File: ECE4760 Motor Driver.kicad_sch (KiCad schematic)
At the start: 47 parts, among them J1 IO, J101 Alternative Motor, J2 Motor / Power, J3 UART, U1 STM32G473V_B-C-E_Hx, U6 AP7361C-33FGE, U7 TPSM365R6, X1 48MHz

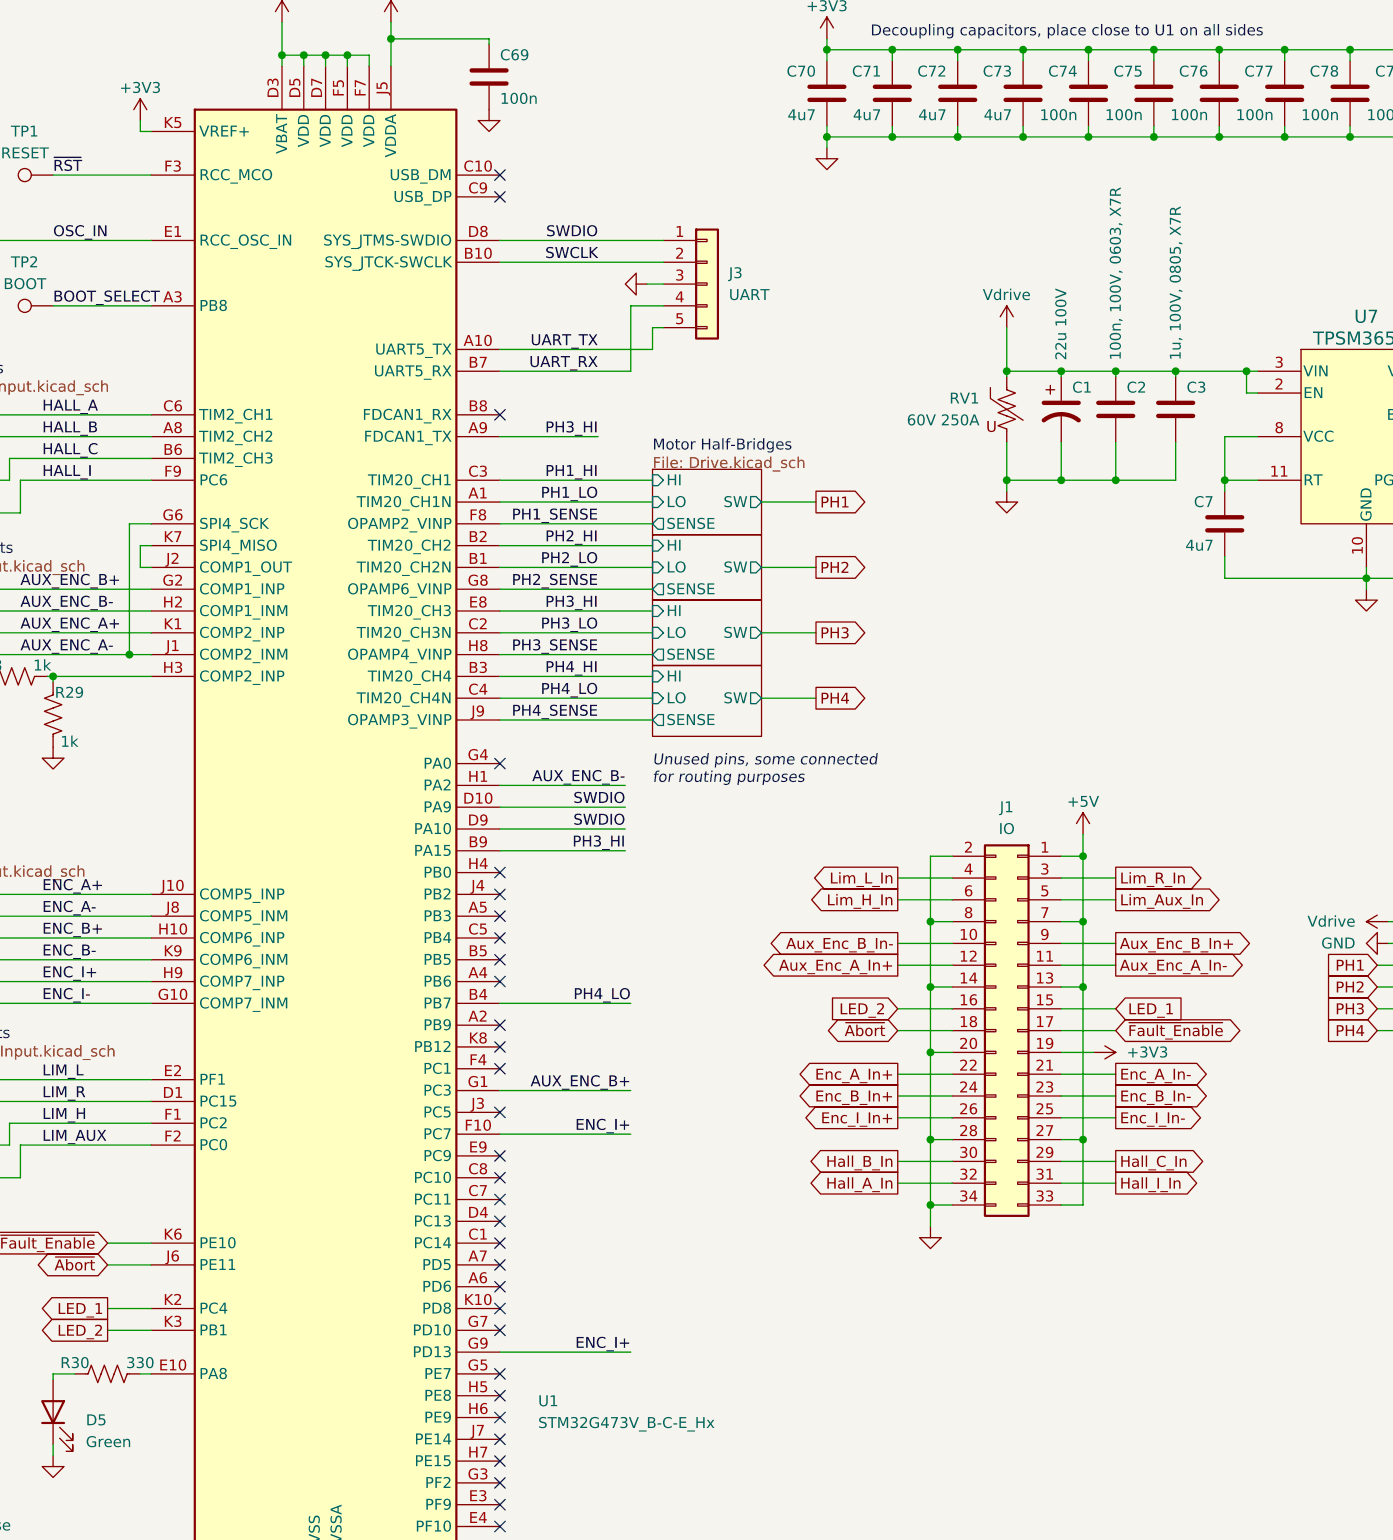
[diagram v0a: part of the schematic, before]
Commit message: Tweaking pin assignments
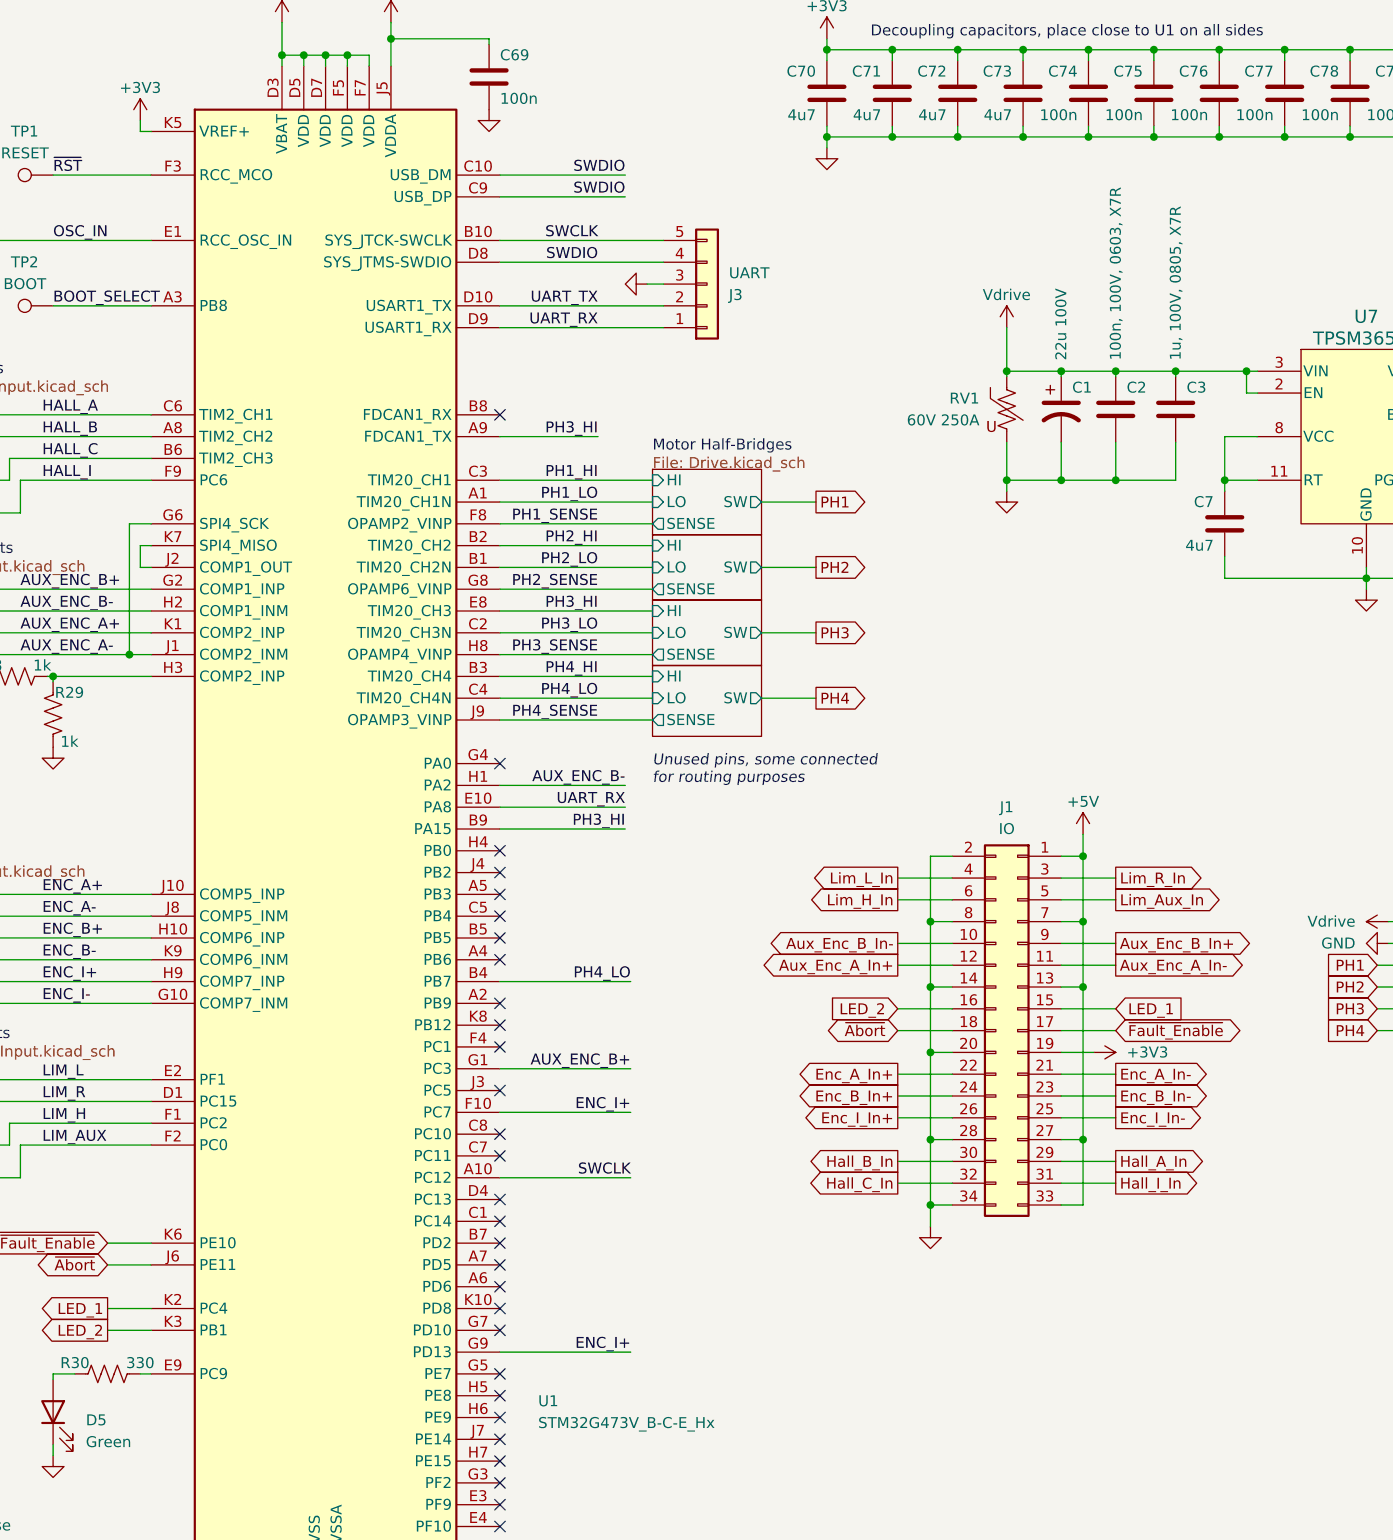
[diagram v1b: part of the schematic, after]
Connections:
- net Hall_A_In: now also J1.29 (Pin_29); no longer J1.32 (Pin_32)
- net Hall_C_In: now also J1.32 (Pin_32); no longer J1.29 (Pin_29)
- net SWCLK: now also J3.5 (Pin_5), U1.A10 (PC12); no longer J3.2 (Pin_2)
- net SWDIO: now also J3.4 (Pin_4), U1.C10 (PA11), U1.C9 (PA12); no longer J3.1 (Pin_1), U1.D10 (PA9), U1.D9 (PA10)
- net UART_RX: now also J3.1 (Pin_1), U1.D9 (PA10), U1.E10 (PA8); no longer J3.4 (Pin_4), U1.B7 (PD2)
- net UART_TX: now also J3.2 (Pin_2), U1.D10 (PA9); no longer J3.5 (Pin_5), U1.A10 (PC12)
- net at R30.2: now also U1.E9 (PC9); no longer U1.E10 (PA8)
- no-connect marks 33 -> 31

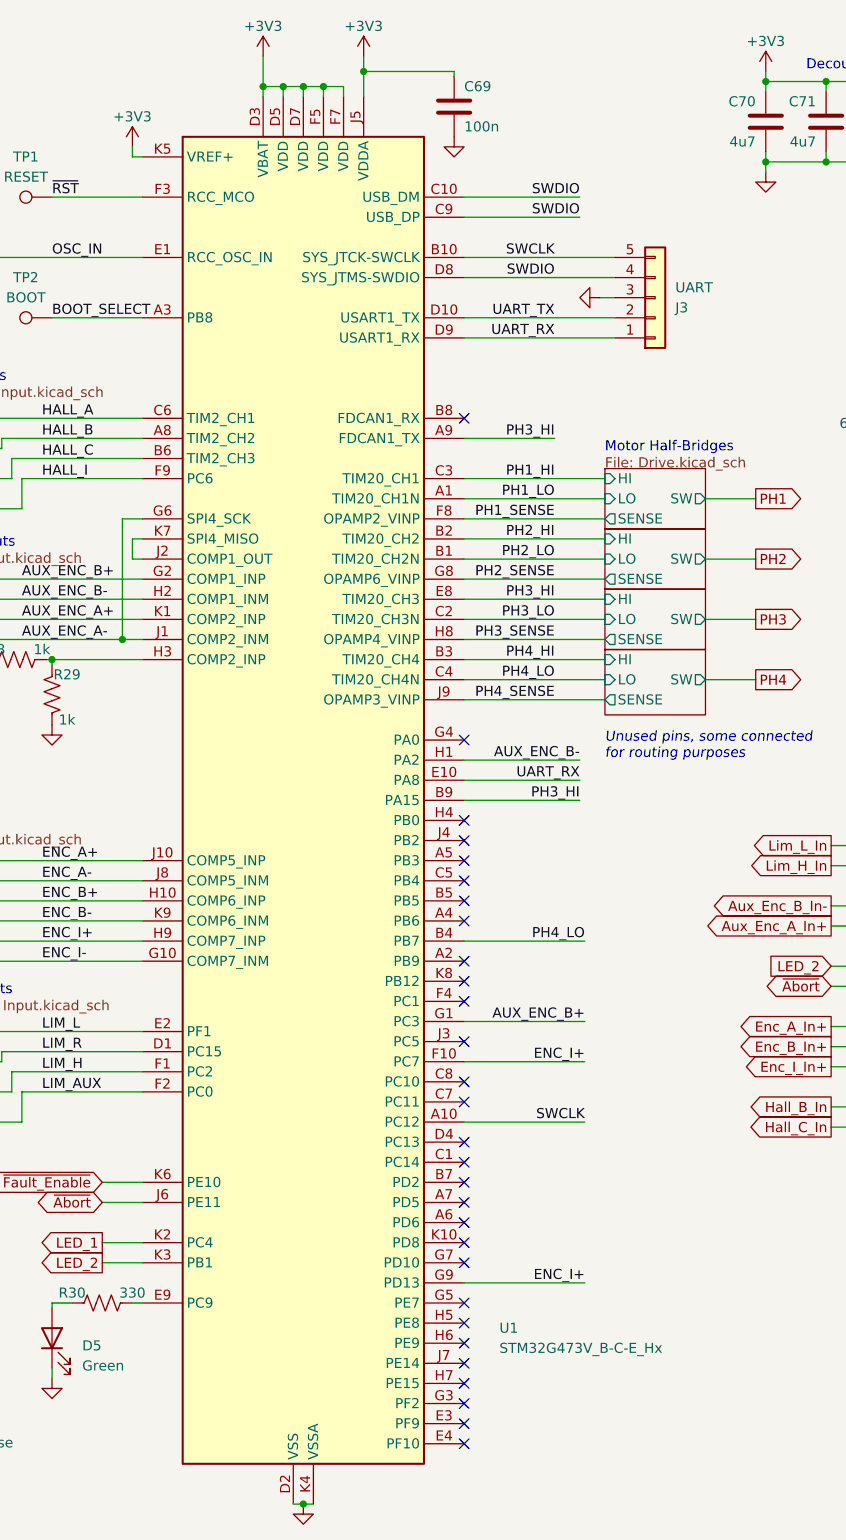
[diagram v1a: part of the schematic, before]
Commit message: Change MCU package and MOSFETs
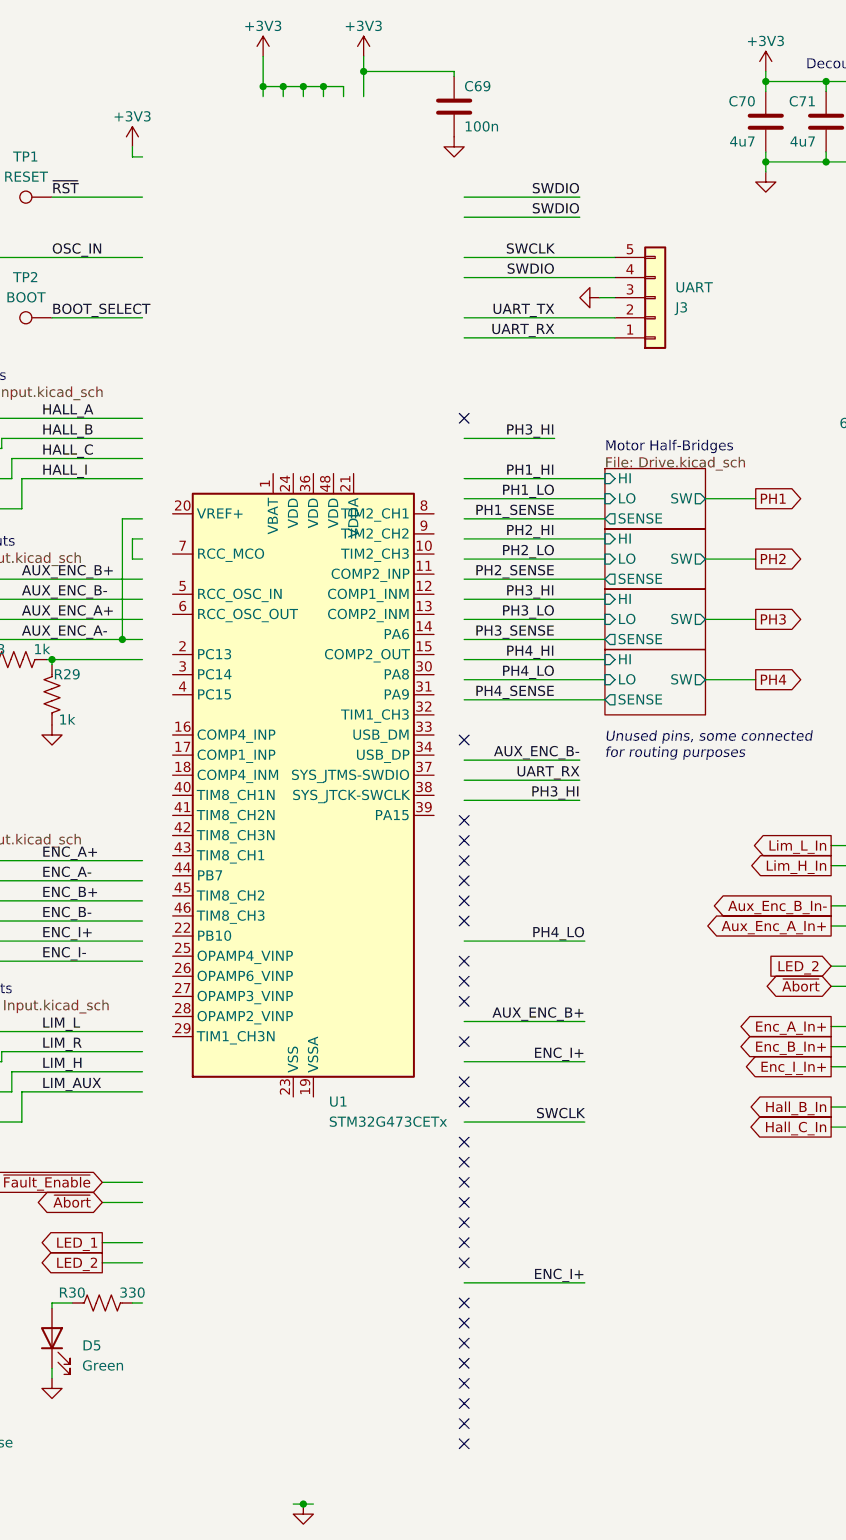
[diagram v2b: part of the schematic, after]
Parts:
- removed U1: STM32G473V_B-C-E_Hx, Package_BGA:TFBGA-100_8x8mm_Layout10x10_P0.8mm, symbol MCU_ST_STM32G4:STM32G473V_B-C-E_Hx
- added U1: STM32G473CETx, Package_QFP:LQFP-48_7x7mm_P0.5mm, symbol MCU_ST_STM32G4:STM32G473CETx
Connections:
- new net: U1.23 (VSS), U1.35 (VSS), U1.47 (VSS)
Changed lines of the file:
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@@
-    )
-  )
-  (symbol (lib_id "MCU_ST_STM32G4:STM32G473V_B-C-E_Hx") (at 88.9 93.345 0) (unit 1)
-    (in_bom yes) (on_board yes) (dnp no)
-    (property "Reference" "U1" (at 113.665 177.8 0)
-      (effects (font (size 1.27 1.27)) (justify left))
-    )
-    (property "Value" "STM32G473V_B-C-E_Hx" (at 113.665 180.34 0)
-      (effects (font (size 1.27 1.27)) (justify left))
-    )
-    (property "Footprint" "Package_BGA:TFBGA-100_8x8mm_Layout10x10_P0.8mm" (at 73.66 159.385 0)
-      (effects (font (size 1.27 1.27)) (justify right) hide)
-    )
-    (property "Datasheet" "https://www.st.com/resource/en/datasheet/stm32g473vb.pdf" (at 88.9 93.345 0)
-      (effects (font (size 1.27 1.27)) hide)
-    )
-    (property "DigiKey" "497-STM32G474VEH6-ND" (at 88.9 93.345 0)
-      (effects (font (size 1.27 1.27)) hide)
-    )
-    (property "Comments" "Any STM32G473, 474, 483, 484 with TFBGA-100 package" (at 88.9 93.345 0)
-      (effects (font (size 1.27 1.27)) hide)
-    )
-    (property "LCSC" "" (at 88.9 93.345 0)
-      (effects (font (size 1.27 1.27)) hide)
-    )
-    (pin "A1" (alternate "TIM20_CH1N"))
-    (pin "A10")
-    (pin "A2")
-    (pin "A3")
-    (pin "A4")
-    (pin "A5")
-    (pin "A6")
-    (pin "A7")
-    (pin "A8" (alternate "TIM2_CH2"))
-    (pin "A9" (alternate "FDCAN1_TX"))
-    (pin "B1" (alternate "TIM20_CH2N"))
-    (pin "B10" (alternate "SYS_JTCK-SWCLK"))
-    (pin "B2" (alternate "TIM20_CH2"))
-    (pin "B3" (alternate "TIM20_CH4"))
-    (pin "B4")
-    (pin "B5")
-    (pin "B6" (alternate "TIM2_CH3"))
-    (pin "B7")
-    (pin "B8" (alternate "FDCAN1_RX"))
-    (pin "B9")
-    (pin "C1")
-    (pin "C10" (alternate "USB_DM"))
-    (pin "C2" (alternate "TIM20_CH3N"))
-    (pin "C3" (alternate "TIM20_CH1"))
-    (pin "C4" (alternate "TIM20_CH4N"))
-    (pin "C5")
-    (pin "C6" (alternate "TIM2_CH1"))
-    (pin "C7")
-    (pin "C8")
-    (pin "C9" (alternate "USB_DP"))
-    (pin "D1")
-    (pin "D10" (alternate "USART1_TX"))
-    (pin "D2")
-    (pin "D3")
-    (pin "D4")
-    (pin "D5")
-    (pin "D6")
-    (pin "D7")
-    (pin "D8" (alternate "SYS_JTMS-SWDIO"))
-    (pin "D9" (alternate "USART1_RX"))
-    (pin "E1" (alternate "RCC_OSC_IN"))
-    (pin "E10")
-    (pin "E2")
-    (pin "E3")
-    (pin "E4")
-    (pin "E5")
-    (pin "E6")
-    (pin "E7")
-    (pin "E8" (alternate "TIM20_CH3"))
-    (pin "E9")
-    (pin "F1")
-    (pin "F10")
-    (pin "F2")
-    (pin "F3" (alternate "RCC_MCO"))
-    (pin "F4")
-    (pin "F5")
-    (pin "F6")
-    (pin "F7")
-    (pin "F8" (alternate "OPAMP2_VINP"))
-    (pin "F9")
-    (pin "G1")
-    (pin "G10" (alternate "COMP7_INM"))
-    (pin "G2" (alternate "COMP1_INP"))
-    (pin "G3")
-    (pin "G4")
-    (pin "G5")
-    (pin "G6" (alternate "SPI4_SCK"))
-    (pin "G7")
-    (pin "G8" (alternate "OPAMP6_VINP"))
-    (pin "G9")
-    (pin "H1")
-    (pin "H10" (alternate "COMP6_INP"))
-    (pin "H2" (alternate "COMP1_INM"))
-    (pin "H3" (alternate "COMP2_INP"))
-    (pin "H4")
-    (pin "H5")
-    (pin "H6")
-    (pin "H7")
-    (pin "H8" (alternate "OPAMP4_VINP"))
-    (pin "H9" (alternate "COMP7_INP"))
-    (pin "J1" (alternate "COMP2_INM"))
-    (pin "J10" (alternate "COMP5_INP"))
-    (pin "J2" (alternate "COMP1_OUT"))
-    (pin "J3")
-    (pin "J4")
-    (pin "J5")
-    (pin "J6")
-    (pin "J7")
-    (pin "J8" (alternate "COMP5_INM"))
-    (pin "J9" (alternate "OPAMP3_VINP"))
-    (pin "K1" (alternate "COMP2_INP"))
-    (pin "K10")
-    (pin "K2")
-    (pin "K3")
-    (pin "K4")
-    (pin "K5")
-    (pin "K6")
-    (pin "K7" (alternate "SPI4_MISO"))
-    (pin "K8")
-    (pin "K9" (alternate "COMP6_INM"))
-    (instances
-      (project "ECE4760 Motor Driver"
-        (path "/6b38a626-de8c-4b2d-bc76-3a02bc823a86"
-          (reference "U1") (unit 1)
-        )
-      )
     )
   )
@@
         )
       )
+    )
+  )
+  (symbol (lib_id "MCU_ST_STM32G4:STM32G473CETx") (at 87.63 110.49 0) (unit 1)
+    (in_bom yes) (on_board yes) (dnp no) (fields_autoplaced)
+    (property "Reference" "U1" (at 92.1259 149.225 0)
+      (effects (font (size 1.27 1.27)) (justify left))
+    )
+    (property "Value" "STM32G473CETx" (at 92.1259 151.765 0)
+      (effects (font (size 1.27 1.27)) (justify left))
+    )
+    (property "Footprint" "Package_QFP:LQFP-48_7x7mm_P0.5mm" (at 74.93 146.05 0)
+      (effects (font (size 1.27 1.27)) (justify right) hide)
+    )
+    (property "Datasheet" "https://www.st.com/resource/en/datasheet/stm32g473ce.pdf" (at 87.63 110.49 0)
+      (effects (font (size 1.27 1.27)) hide)
+    )
+    (pin "1")
+    (pin "10" (alternate "TIM2_CH3"))
+    (pin "11" (alternate "COMP2_INP"))
+    (pin "12" (alternate "COMP1_INM"))
+    (pin "13" (alternate "COMP2_INM"))
+    (pin "14")
+    (pin "15" (alternate "COMP2_OUT"))
+    (pin "16" (alternate "COMP4_INP"))
+    (pin "17" (alternate "COMP1_INP"))
+    (pin "18" (alternate "COMP4_INM"))
+    (pin "19")
+    (pin "2")
+    (pin "20")
+    (pin "21")
+    (pin "22")
+    (pin "23")
+    (pin "24")
+    (pin "25" (alternate "OPAMP4_VINP"))
+    (pin "26" (alternate "OPAMP6_VINP"))
+    (pin "27" (alternate "OPAMP3_VINP"))
+    (pin "28" (alternate "OPAMP2_VINP"))
+    (pin "29" (alternate "TIM1_CH3N"))
+    (pin "3")
+    (pin "30")
+    (pin "31")
+    (pin "32" (alternate "TIM1_CH3"))
+    (pin "33" (alternate "USB_DM"))
+    (pin "34" (alternate "USB_DP"))
+    (pin "35")
+    (pin "36")
+    (pin "37" (alternate "SYS_JTMS-SWDIO"))
+    (pin "38" (alternate "SYS_JTCK-SWCLK"))
+    (pin "39")
+    (pin "4")
+    (pin "40" (alternate "TIM8_CH1N"))
+    (pin "41" (alternate "TIM8_CH2N"))
+    (pin "42" (alternate "TIM8_CH3N"))
+    (pin "43" (alternate "TIM8_CH1"))
+    (pin "44")
+    (pin "45" (alternate "TIM8_CH2"))
+    (pin "46" (alternate "TIM8_CH3"))
+    (pin "47")
+    (pin "48")
+    (pin "5" (alternate "RCC_OSC_IN"))
+    (pin "6" (alternate "RCC_OSC_OUT"))
+    (pin "7" (alternate "RCC_MCO"))
+    (pin "8" (alternate "TIM2_CH1"))
+    (pin "9" (alternate "TIM2_CH2"))
+    (instances
+      (project "ECE4760 Motor Driver"
+        (path "/6b38a626-de8c-4b2d-bc76-3a02bc823a86"
+          (reference "U1") (unit 1)
+        )
+      )
